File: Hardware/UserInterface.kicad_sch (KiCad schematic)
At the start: 24 parts, among them U2 74HC595, U3 74HC595, U4 74HC595, U5 74HC595, U6 74HC595

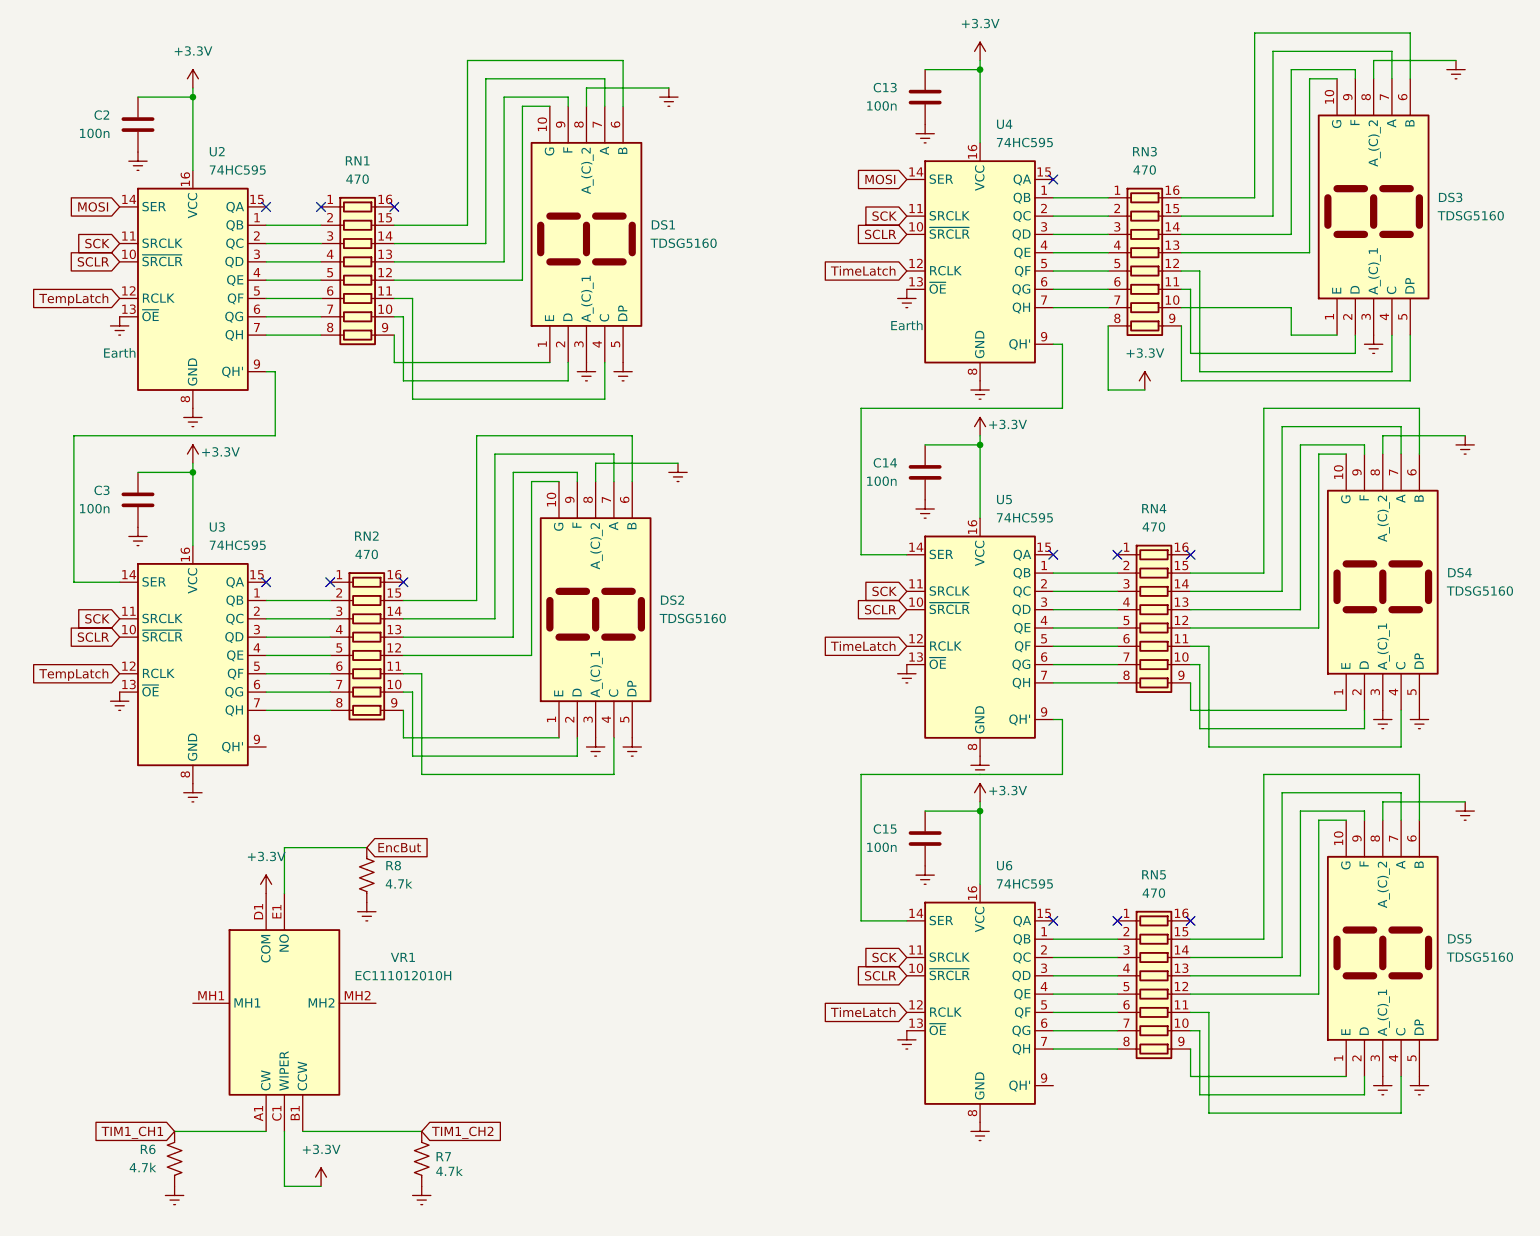
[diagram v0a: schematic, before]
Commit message: added footprints
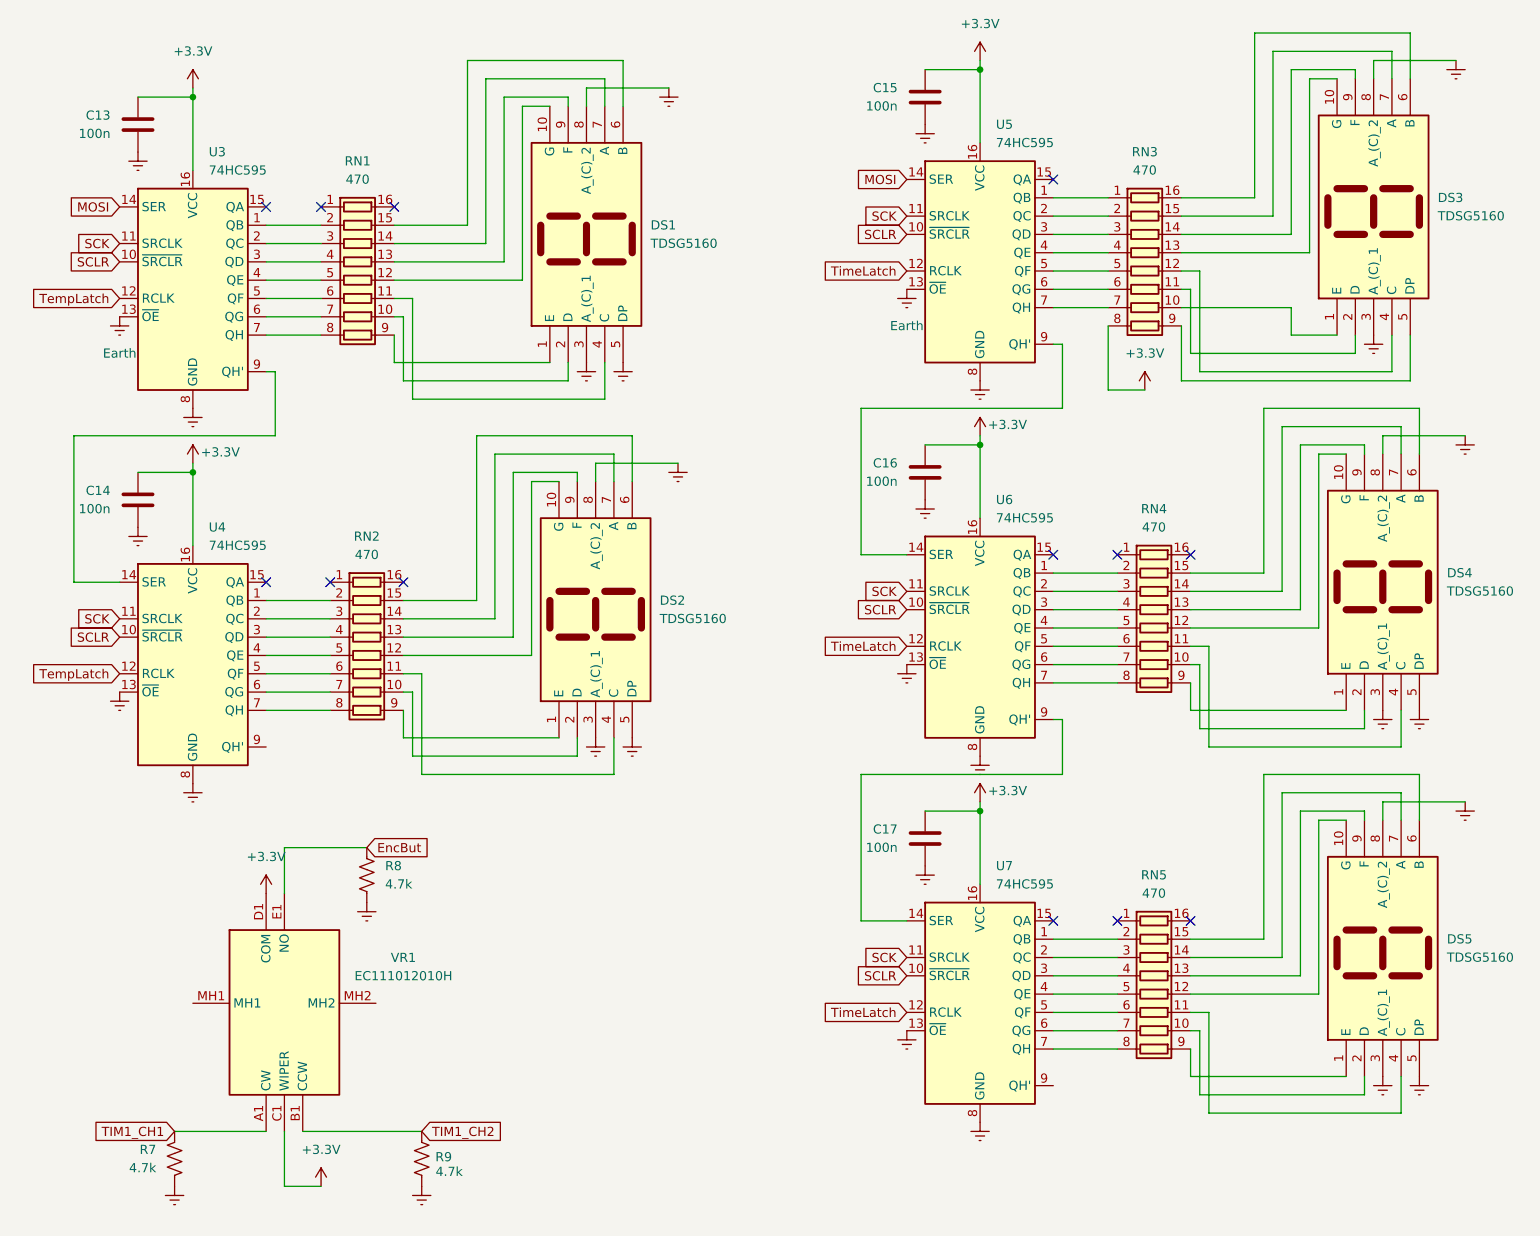
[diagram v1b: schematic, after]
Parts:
- C13: renamed from C2; footprint (none) -> Capacitor_SMD:C_0805_2012Metric
- C14: renamed from C3; footprint (none) -> Capacitor_SMD:C_0805_2012Metric
- C15: renamed from C13; footprint (none) -> Capacitor_SMD:C_0805_2012Metric
- C16: renamed from C14; footprint (none) -> Capacitor_SMD:C_0805_2012Metric
- C17: renamed from C15; footprint (none) -> Capacitor_SMD:C_0805_2012Metric
- R7: renamed from R6; footprint (none) -> Resistor_SMD:R_0805_2012Metric
- R8: footprint (none) -> Resistor_SMD:R_0805_2012Metric
- R9: renamed from R7; footprint (none) -> Resistor_SMD:R_0805_2012Metric
- U3: renamed from U2; footprint (none) -> SamacSys_Parts:SOIC127P600X175-16N
- U4: renamed from U3; footprint (none) -> SamacSys_Parts:SOIC127P600X175-16N
- U5: renamed from U4; footprint (none) -> SamacSys_Parts:SOIC127P600X175-16N
- U6: renamed from U5; footprint (none) -> SamacSys_Parts:SOIC127P600X175-16N
- U7: renamed from U6; footprint (none) -> SamacSys_Parts:SOIC127P600X175-16N

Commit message: Added temperature sensor and I2C setup, started PCB layout
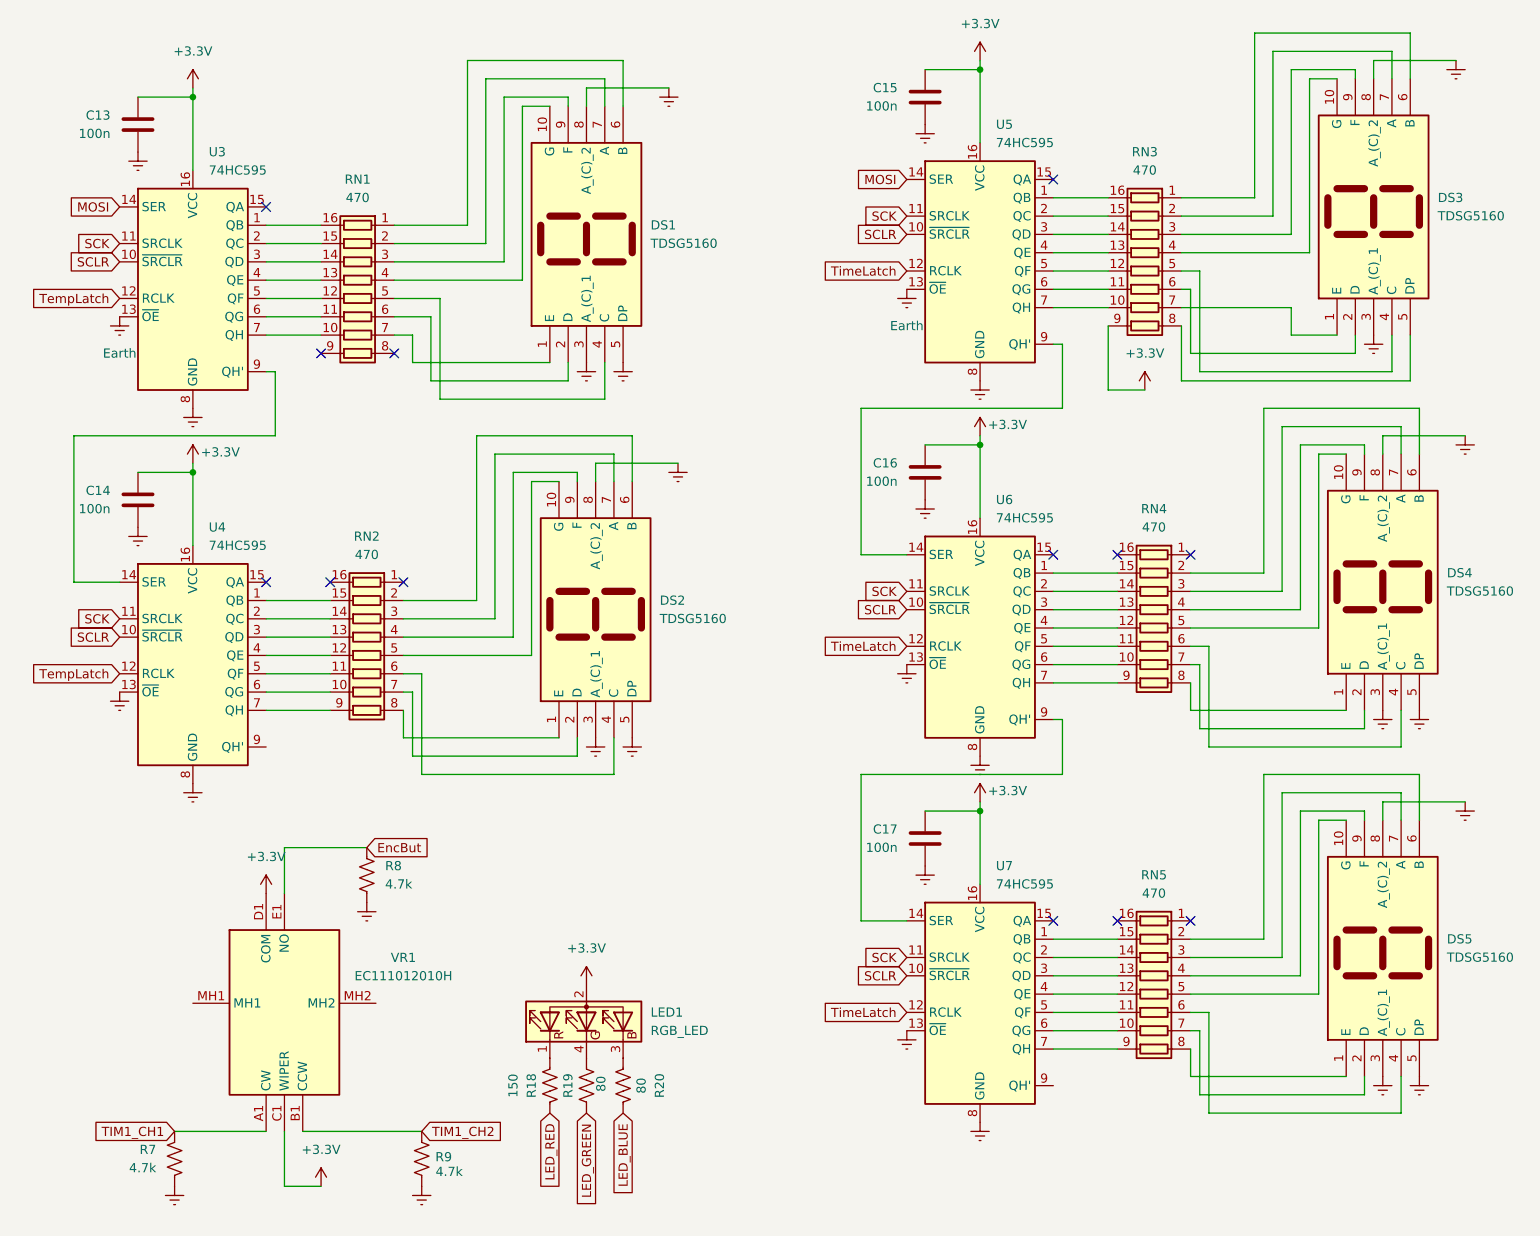
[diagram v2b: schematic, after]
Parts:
- added LED1: RGB_LED, SamacSys_Parts:5218559F, symbol Device:LED_ARBG
- added R18: 150, Resistor_SMD:R_0805_2012Metric, symbol Device:R_US
- added R19, R20: 80, Resistor_SMD:R_0805_2012Metric, symbol Device:R_US
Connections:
- net +3.3V: now also RN3.9 (R8.2), LED1.2 (A); no longer RN3.8 (R8.1)
- net at U7.1 (QB): now also RN5.15 (R2.2); no longer RN5.2 (R2.1)
- net at U7.2 (QC): now also RN5.14 (R3.2); no longer RN5.3 (R3.1)
- net at U7.3 (QD): now also RN5.13 (R4.2); no longer RN5.4 (R4.1)
- net at U7.4 (QE): now also RN5.12 (R5.2); no longer RN5.5 (R5.1)
- net at U7.5 (QF): now also RN5.11 (R6.2); no longer RN5.6 (R6.1)
- net at U7.6 (QG): now also RN5.10 (R7.2); no longer RN5.7 (R7.1)
- net at U7.7 (QH): now also RN5.9 (R8.2); no longer RN5.8 (R8.1)
- net at U6.1 (QB): now also RN4.15 (R2.2); no longer RN4.2 (R2.1)
- net at U6.2 (QC): now also RN4.14 (R3.2); no longer RN4.3 (R3.1)
- net at U6.3 (QD): now also RN4.13 (R4.2); no longer RN4.4 (R4.1)
- net at U6.4 (QE): now also RN4.12 (R5.2); no longer RN4.5 (R5.1)
- net at U6.5 (QF): now also RN4.11 (R6.2); no longer RN4.6 (R6.1)
- net at U6.6 (QG): now also RN4.10 (R7.2); no longer RN4.7 (R7.1)
- net at U6.7 (QH): now also RN4.9 (R8.2); no longer RN4.8 (R8.1)
- net at DS4.1 (E): now also RN4.8 (R8.1); no longer RN4.9 (R8.2)
- net at DS4.10 (G): now also RN4.5 (R5.1); no longer RN4.12 (R5.2)
- net at DS4.2 (D): now also RN4.7 (R7.1); no longer RN4.10 (R7.2)
- net at DS4.4 (C): now also RN4.6 (R6.1); no longer RN4.11 (R6.2)
- net at DS4.6 (B): now also RN4.2 (R2.1); no longer RN4.15 (R2.2)
- net at DS4.7 (A): now also RN4.3 (R3.1); no longer RN4.14 (R3.2)
- net at DS4.9 (F): now also RN4.4 (R4.1); no longer RN4.13 (R4.2)
- net at RN2.10 (R7.2): now also U4.6 (QG); no longer DS2.2 (D)
- net at RN2.11 (R6.2): now also U4.5 (QF); no longer DS2.4 (C)
- net at RN2.12 (R5.2): now also U4.4 (QE); no longer DS2.10 (G)
- net at RN2.13 (R4.2): now also U4.3 (QD); no longer DS2.9 (F)
- net at RN2.14 (R3.2): now also U4.2 (QC); no longer DS2.7 (A)
- net at RN2.15 (R2.2): now also U4.1 (QB); no longer DS2.6 (B)
- net at RN2.2 (R2.1): now also DS2.6 (B); no longer U4.1 (QB)
- net at RN2.3 (R3.1): now also DS2.7 (A); no longer U4.2 (QC)
- net at RN2.4 (R4.1): now also DS2.9 (F); no longer U4.3 (QD)
- net at RN2.5 (R5.1): now also DS2.10 (G); no longer U4.4 (QE)
- net at RN2.6 (R6.1): now also DS2.4 (C); no longer U4.5 (QF)
- net at RN2.7 (R7.1): now also DS2.2 (D); no longer U4.6 (QG)
- net at RN2.8 (R8.1): now also DS2.1 (E); no longer U4.7 (QH)
- net at RN2.9 (R8.2): now also U4.7 (QH); no longer DS2.1 (E)
- net at DS5.1 (E): now also RN5.8 (R8.1); no longer RN5.9 (R8.2)
- net at DS5.10 (G): now also RN5.5 (R5.1); no longer RN5.12 (R5.2)
- net at DS5.2 (D): now also RN5.7 (R7.1); no longer RN5.10 (R7.2)
- net at DS5.4 (C): now also RN5.6 (R6.1); no longer RN5.11 (R6.2)
- net at DS5.6 (B): now also RN5.2 (R2.1); no longer RN5.15 (R2.2)
- net at DS5.7 (A): now also RN5.3 (R3.1); no longer RN5.14 (R3.2)
- net at DS5.9 (F): now also RN5.4 (R4.1); no longer RN5.13 (R4.2)
- net at RN1.1 (R1.1): now also DS1.6 (B)
- net at RN1.10 (R7.2): now also U3.7 (QH); no longer DS1.2 (D)
- net at RN1.11 (R6.2): now also U3.6 (QG); no longer DS1.4 (C)
- net at RN1.12 (R5.2): now also U3.5 (QF); no longer DS1.10 (G)
- net at RN1.13 (R4.2): now also U3.4 (QE); no longer DS1.9 (F)
- net at RN1.14 (R3.2): now also U3.3 (QD); no longer DS1.7 (A)
- net at RN1.15 (R2.2): now also U3.2 (QC); no longer DS1.6 (B)
- net at RN1.16 (R1.2): now also U3.1 (QB)
- net at RN1.2 (R2.1): now also DS1.7 (A); no longer U3.1 (QB)
- net at RN1.3 (R3.1): now also DS1.9 (F); no longer U3.2 (QC)
- net at RN1.4 (R4.1): now also DS1.10 (G); no longer U3.3 (QD)
- net at RN1.5 (R5.1): now also DS1.4 (C); no longer U3.4 (QE)
- net at RN1.6 (R6.1): now also DS1.2 (D); no longer U3.5 (QF)
- net at RN1.7 (R7.1): now also DS1.1 (E); no longer U3.6 (QG)
- net at RN1.8 (R8.1): no longer U3.7 (QH)
- net at RN1.9 (R8.2): no longer DS1.1 (E)
- net at U5.1 (QB): now also RN3.16 (R1.2); no longer RN3.1 (R1.1)
- net at U5.2 (QC): now also RN3.15 (R2.2); no longer RN3.2 (R2.1)
- net at U5.3 (QD): now also RN3.14 (R3.2); no longer RN3.3 (R3.1)
- net at U5.4 (QE): now also RN3.13 (R4.2); no longer RN3.4 (R4.1)
- net at U5.5 (QF): now also RN3.12 (R5.2); no longer RN3.5 (R5.1)
- net at U5.6 (QG): now also RN3.11 (R6.2); no longer RN3.6 (R6.1)
- net at U5.7 (QH): now also RN3.10 (R7.2); no longer RN3.7 (R7.1)
- net at DS3.1 (E): now also RN3.7 (R7.1); no longer RN3.10 (R7.2)
- net at DS3.10 (G): now also RN3.4 (R4.1); no longer RN3.13 (R4.2)
- net at DS3.2 (D): now also RN3.6 (R6.1); no longer RN3.11 (R6.2)
- net at DS3.4 (C): now also RN3.5 (R5.1); no longer RN3.12 (R5.2)
- net at DS3.5 (DP): now also RN3.8 (R8.1); no longer RN3.9 (R8.2)
- net at DS3.6 (B): now also RN3.1 (R1.1); no longer RN3.16 (R1.2)
- net at DS3.7 (A): now also RN3.2 (R2.1); no longer RN3.15 (R2.2)
- net at DS3.9 (F): now also RN3.3 (R3.1); no longer RN3.14 (R3.2)
- new net: LED1.4 (GK), R19.1
- new net: LED1.1, R18.1
- new net: LED1.3 (BK), R20.2
- new net LED_BLUE: R20.1
- new net LED_GREEN: R19.2
- new net LED_RED: R18.2
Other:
- moved on the sheet: RN1, RN2, RN3, RN4, RN5

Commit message: Almost finished PCB
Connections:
- net at U7.1 (QB): now also RN5.16 (R1.2); no longer RN5.15 (R2.2)
- net at U7.2 (QC): now also RN5.15 (R2.2); no longer RN5.14 (R3.2)
- net at U7.3 (QD): now also RN5.14 (R3.2); no longer RN5.13 (R4.2)
- net at U7.4 (QE): now also RN5.13 (R4.2); no longer RN5.12 (R5.2)
- net at U7.5 (QF): now also RN5.12 (R5.2); no longer RN5.11 (R6.2)
- net at U7.6 (QG): now also RN5.11 (R6.2); no longer RN5.10 (R7.2)
- net at U7.7 (QH): now also RN5.10 (R7.2); no longer RN5.9 (R8.2)
- net at U6.1 (QB): now also RN4.16 (R1.2); no longer RN4.15 (R2.2)
- net at U6.2 (QC): now also RN4.15 (R2.2); no longer RN4.14 (R3.2)
- net at U6.3 (QD): now also RN4.14 (R3.2); no longer RN4.13 (R4.2)
- net at U6.4 (QE): now also RN4.13 (R4.2); no longer RN4.12 (R5.2)
- net at U6.5 (QF): now also RN4.12 (R5.2); no longer RN4.11 (R6.2)
- net at U6.6 (QG): now also RN4.11 (R6.2); no longer RN4.10 (R7.2)
- net at U6.7 (QH): now also RN4.10 (R7.2); no longer RN4.9 (R8.2)
- net at DS4.1 (E): now also RN4.1 (R1.1); no longer RN4.8 (R8.1)
- net at DS4.10 (G): now also RN4.4 (R4.1); no longer RN4.5 (R5.1)
- net at DS4.2 (D): now also RN4.2 (R2.1); no longer RN4.7 (R7.1)
- net at DS4.4 (C): now also RN4.3 (R3.1); no longer RN4.6 (R6.1)
- net at DS4.6 (B): now also RN4.7 (R7.1); no longer RN4.2 (R2.1)
- net at DS4.7 (A): now also RN4.6 (R6.1); no longer RN4.3 (R3.1)
- net at DS4.9 (F): now also RN4.5 (R5.1); no longer RN4.4 (R4.1)
- net at RN2.1 (R1.1): now also DS2.1 (E)
- net at RN2.10 (R7.2): now also U4.7 (QH); no longer U4.6 (QG)
- net at RN2.11 (R6.2): now also U4.6 (QG); no longer U4.5 (QF)
- net at RN2.12 (R5.2): now also U4.5 (QF); no longer U4.4 (QE)
- net at RN2.13 (R4.2): now also U4.4 (QE); no longer U4.3 (QD)
- net at RN2.14 (R3.2): now also U4.3 (QD); no longer U4.2 (QC)
- net at RN2.15 (R2.2): now also U4.2 (QC); no longer U4.1 (QB)
- net at RN2.16 (R1.2): now also U4.1 (QB)
- net at RN2.2 (R2.1): now also DS2.2 (D); no longer DS2.6 (B)
- net at RN2.3 (R3.1): now also DS2.4 (C); no longer DS2.7 (A)
- net at RN2.4 (R4.1): now also DS2.10 (G); no longer DS2.9 (F)
- net at RN2.5 (R5.1): now also DS2.9 (F); no longer DS2.10 (G)
- net at RN2.6 (R6.1): now also DS2.7 (A); no longer DS2.4 (C)
- net at RN2.7 (R7.1): now also DS2.6 (B); no longer DS2.2 (D)
- net at RN2.8 (R8.1): no longer DS2.1 (E)
- net at RN2.9 (R8.2): no longer U4.7 (QH)
- net at DS5.1 (E): now also RN5.1 (R1.1); no longer RN5.8 (R8.1)
- net at DS5.10 (G): now also RN5.4 (R4.1); no longer RN5.5 (R5.1)
- net at DS5.2 (D): now also RN5.2 (R2.1); no longer RN5.7 (R7.1)
- net at DS5.4 (C): now also RN5.3 (R3.1); no longer RN5.6 (R6.1)
- net at DS5.6 (B): now also RN5.7 (R7.1); no longer RN5.2 (R2.1)
- net at DS5.7 (A): now also RN5.6 (R6.1); no longer RN5.3 (R3.1)
- net at DS5.9 (F): now also RN5.5 (R5.1); no longer RN5.4 (R4.1)
- net at RN1.1 (R1.1): now also DS1.1 (E); no longer DS1.6 (B)
- net at RN1.2 (R2.1): now also DS1.2 (D); no longer DS1.7 (A)
- net at RN1.3 (R3.1): now also DS1.4 (C); no longer DS1.9 (F)
- net at RN1.5 (R5.1): now also DS1.9 (F); no longer DS1.4 (C)
- net at RN1.6 (R6.1): now also DS1.7 (A); no longer DS1.2 (D)
- net at RN1.7 (R7.1): now also DS1.6 (B); no longer DS1.1 (E)
- net at DS3.1 (E): now also RN3.1 (R1.1); no longer RN3.7 (R7.1)
- net at DS3.2 (D): now also RN3.2 (R2.1); no longer RN3.6 (R6.1)
- net at DS3.4 (C): now also RN3.3 (R3.1); no longer RN3.5 (R5.1)
- net at DS3.6 (B): now also RN3.7 (R7.1); no longer RN3.1 (R1.1)
- net at DS3.7 (A): now also RN3.6 (R6.1); no longer RN3.2 (R2.1)
- net at DS3.9 (F): now also RN3.5 (R5.1); no longer RN3.3 (R3.1)
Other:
- moved on the sheet: C17, DS5, RN2, RN4, RN5, U7
